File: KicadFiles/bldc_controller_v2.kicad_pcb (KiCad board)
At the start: 4 copper layers, 51.5 x 89 mm, 172 parts, among them J1 Conn_01x05_Male, J10 Conn_01x02_Female, J11 Conn_01x02_Female, J12 Conn_01x02_Female, J13 Conn_01x02_Female, J14 Conn_01x02_Female, J15 Conn_01x04_Male, J2 Conn_01x03_Male, J3 Conn_01x03_Male, J4 1935174, J5 Conn_01x02_Female, J9 Conn_01x02_Female, Q10 IRLB8721PBF, Q11 IRLB8721PBF, Q2 DMN65D8L-7, Q3 DMN65D8L-7, Q5 IRF4905, Q6 IRLB8721PBF, Q7 IRLB8721PBF, Q8 IRLB8721PBF, Q9 IRLB8721PBF, SW2 D6C40 F1 LFS, SW3 1301.9314, SW4 1301.9314, SW5 SW_Push_DPDT, U1 ATmega328P-PU, U2 uA7810, U3 LM7805_TO220, U4 MCP601-xP, U5 LM339, U6 IRS2004, U7 IRS2004, U8 IRS2004, U9 HCPL-181-00DE, Y1 9B-16.000MBBK-B

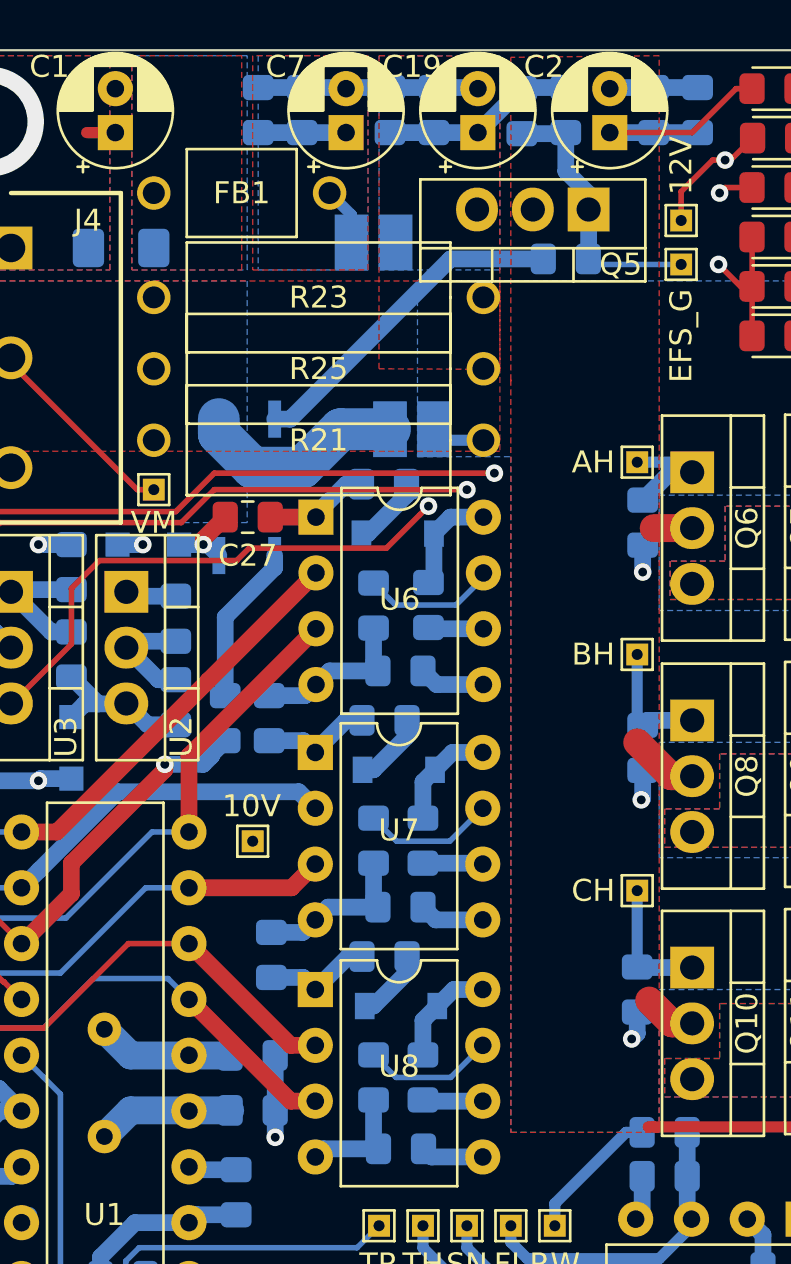
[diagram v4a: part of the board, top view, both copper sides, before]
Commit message: Almost Passes DRC
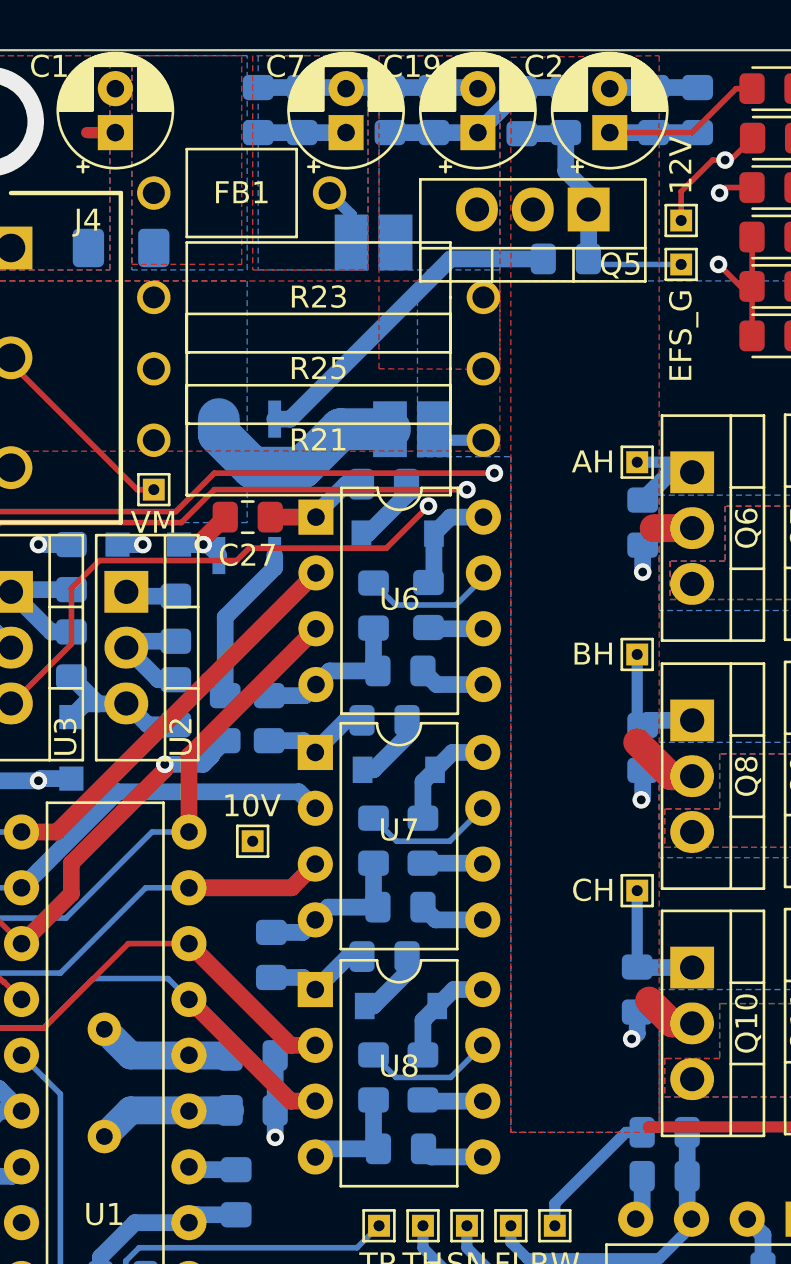
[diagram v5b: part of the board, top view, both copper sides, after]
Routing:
- net +5V: track 105.6 -> 106.7 mm
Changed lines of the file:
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@@
     (thickness 1.6)
     (drawings 76)
-    (tracks 751)
+    (tracks 753)
     (zones 0)
     (modules 172)
@@
     (35 F.Paste user)
     (36 B.SilkS user)
-    (37 F.SilkS user hide)
+    (37 F.SilkS user)
     (38 B.Mask user hide)
     (39 F.Mask user hide)
@@
   )
   (setup
-    (last_trace_width 1.27)
+    (last_trace_width 0.254)
     (user_trace_width 0.254)
     (user_trace_width 0.508)
@@
       (effects (font (size 1 1) (thickness 0.15)))
     )
+    (fp_line (start 1 1) (end -1 1) (layer F.CrtYd) (width 0.05))
+    (fp_line (start 1 1) (end 1 -1) (layer F.CrtYd) (width 0.05))
+    (fp_line (start -1 -1) (end -1 1) (layer F.CrtYd) (width 0.05))
+    (fp_line (start -1 -1) (end 1 -1) (layer F.CrtYd) (width 0.05))
+    (fp_line (start -0.7 0.7) (end -0.7 -0.7) (layer F.SilkS) (width 0.12))
+    (fp_line (start 0.7 0.7) (end -0.7 0.7) (layer F.SilkS) (width 0.12))
+    (fp_line (start 0.7 -0.7) (end 0.7 0.7) (layer F.SilkS) (width 0.12))
+    (fp_line (start -0.7 -0.7) (end 0.7 -0.7) (layer F.SilkS) (width 0.12))
     (fp_text user %R (at 0 -1.45) (layer F.Fab)
       (effects (font (size 1 1) (thickness 0.15)))
     )
-    (fp_line (start -0.7 -0.7) (end 0.7 -0.7) (layer F.SilkS) (width 0.12))
-    (fp_line (start 0.7 -0.7) (end 0.7 0.7) (layer F.SilkS) (width 0.12))
-    (fp_line (start 0.7 0.7) (end -0.7 0.7) (layer F.SilkS) (width 0.12))
-    (fp_line (start -0.7 0.7) (end -0.7 -0.7) (layer F.SilkS) (width 0.12))
-    (fp_line (start -1 -1) (end 1 -1) (layer F.CrtYd) (width 0.05))
-    (fp_line (start -1 -1) (end -1 1) (layer F.CrtYd) (width 0.05))
-    (fp_line (start 1 1) (end 1 -1) (layer F.CrtYd) (width 0.05))
-    (fp_line (start 1 1) (end -1 1) (layer F.CrtYd) (width 0.05))
     (pad 1 thru_hole rect (at 0 0) (size 1 1) (drill 0.5) (layers *.Cu *.Mask)
       (net 7 +12V))
@@
   (segment (start 117.25 90.73) (end 117.2975 90.73) (width 0.254) (layer F.Cu) (net 6))
   (segment (start 117.2975 90.73) (end 120 88.0275) (width 0.254) (layer F.Cu) (net 6))
-  (segment (start 136.25 72.5) (end 138.001148 70.748852) (width 0.254) (layer In1.Cu) (net 6))
-  (segment (start 136.25 81.75) (end 136.25 72.5) (width 0.254) (layer In1.Cu) (net 6))
-  (segment (start 138.001148 70.748852) (end 148.886164 70.748852) (width 0.254) (layer In1.Cu) (net 6))
-  (segment (start 148.886164 70.748852) (end 149.451849 70.748852) (width 0.254) (layer In1.Cu) (net 6))
   (via (at 149.451849 70.748852) (size 0.8) (drill 0.4) (layers F.Cu B.Cu) (net 6))
   (segment (start 150.452997 71.75) (end 149.451849 70.748852) (width 0.254) (layer F.Cu) (net 6))
@@
   (segment (start 116.7 108.25) (end 117.73 109.28) (width 0.762) (layer B.Cu) (net 6))
   (segment (start 114.75 108.25) (end 116.7 108.25) (width 0.762) (layer B.Cu) (net 6))
+  (segment (start 144.498852 70.748852) (end 144.5 70.75) (width 0.254) (layer In1.Cu) (net 6))
+  (segment (start 138.001148 70.748852) (end 144.498852 70.748852) (width 0.254) (layer In1.Cu) (net 6))
+  (segment (start 136.25 81.75) (end 136.25 72.5) (width 0.254) (layer In1.Cu) (net 6))
+  (segment (start 136.25 72.5) (end 138.001148 70.748852) (width 0.254) (layer In1.Cu) (net 6))
+  (segment (start 144.498852 70.748852) (end 145.75 72) (width 0.254) (layer In1.Cu) (net 6))
+  (segment (start 145.75 72) (end 148.25 72) (width 0.254) (layer In1.Cu) (net 6))
+  (segment (start 148.25 71.950701) (end 149.451849 70.748852) (width 0.254) (layer In1.Cu) (net 6))
+  (segment (start 148.25 72) (end 148.25 71.950701) (width 0.254) (layer In1.Cu) (net 6))
   (segment (start 122.7 85.85) (end 122.5 85.65) (width 0.762) (layer B.Cu) (net 7))
   (segment (start 124.75 85.85) (end 122.7 85.85) (width 0.762) (layer B.Cu) (net 7))
@@
   (segment (start 150.975 67.25) (end 149.750006 67.25) (width 0.254) (layer F.Cu) (net 8))
   (segment (start 131.13 76.87) (end 131.13 82.25) (width 0.254) (layer In1.Cu) (net 8))
-  (segment (start 147 67.5) (end 146 68.5) (width 0.254) (layer In1.Cu) (net 8))
-  (segment (start 149.500006 67.5) (end 147 67.5) (width 0.254) (layer In1.Cu) (net 8))
-  (segment (start 146 68.5) (end 146 69.125) (width 0.254) (layer In1.Cu) (net 8))
-  (segment (start 146 69.125) (end 145.125 70) (width 0.254) (layer In1.Cu) (net 8))
-  (segment (start 145.125 70) (end 138 70) (width 0.254) (layer In1.Cu) (net 8))
   (segment (start 138 70) (end 131.13 76.87) (width 0.254) (layer In1.Cu) (net 8))
+  (segment (start 144.5 70) (end 138 70) (width 0.254) (layer In1.Cu) (net 8))
+  (segment (start 149.500006 67.5) (end 147 67.5) (width 0.254) (layer In1.Cu) (net 8))
+  (segment (start 147 67.5) (end 144.5 70) (width 0.254) (layer In1.Cu) (net 8))
   (via (at 119.5 122.5) (size 0.8) (drill 0.4) (layers F.Cu B.Cu) (net 9))
   (segment (start 146.3 140.975) (end 143.9 140.975) (width 0.254) (layer B.Cu) (net 9))
@@
   (segment (start 120 87.475) (end 119.075 87.475) (width 0.762) (layer B.Cu) (net 86))
   (zone (net 2) (net_name +BATT) (layer F.Cu) (hatch edge 0.508)
+    (priority 1)
     (connect_pads (clearance 0.508))
     (min_thickness 0.254)
@@
   )
   (zone (net 2) (net_name +BATT) (layer B.Cu) (hatch edge 0.508)
+    (priority 1)
     (connect_pads (clearance 0.508))
     (min_thickness 0.254)
@@
   )
   (zone (net 32) (net_name "Net-(F1-Pad1)") (layer B.Cu) (hatch edge 0.508)
+    (priority 2)
     (connect_pads (clearance 0.508))
     (min_thickness 0.254)
@@
   )
   (zone (net 32) (net_name "Net-(F1-Pad1)") (layer F.Cu) (hatch edge 0.508)
+    (priority 2)
     (connect_pads (clearance 0.508))
     (min_thickness 0.254)
@@
     (polygon
       (pts
-        (xy 122.75 71) (xy 127.75 71) (xy 127.75 61.25) (xy 122.75 61.25)
+        (xy 122.75 70.75) (xy 127.75 70.75) (xy 127.75 61.25) (xy 122.75 61.25)
       )
     )
   )
   (zone (net 7) (net_name +12V) (layer F.Cu) (hatch edge 0.508)
+    (priority 3)
     (connect_pads (clearance 0.508))
     (min_thickness 0.254)
@@
   )
   (zone (net 7) (net_name +12V) (layer B.Cu) (hatch edge 0.508)
+    (priority 3)
     (connect_pads (clearance 0.508))
     (min_thickness 0.254)
@@
   )
   (zone (net 12) (net_name /V_MOTOR) (layer F.Cu) (hatch edge 0.508)
+    (priority 4)
     (connect_pads (clearance 0.508))
     (min_thickness 0.254)
@@
   )
   (zone (net 45) (net_name /I_RAW) (layer B.Cu) (hatch edge 0.508)
+    (priority 6)
     (connect_pads (clearance 0.508))
     (min_thickness 0.254)
@@
   )
   (zone (net 1) (net_name GNDPWR) (layer Gnd.Cu) (hatch edge 0.508)
+    (priority 10)
     (connect_pads (clearance 0.508))
     (min_thickness 0.254)
@@
     (polygon
       (pts
-        (xy 113.25 82.5) (xy 164.25 82.5) (xy 164.25 63.5) (xy 162 61.25) (xy 115.5 61.25)
+        (xy 113.25 82.5) (xy 164.25 82.5) (xy 164.25 61.25) (xy 162 61.25) (xy 115.5 61.25)
         (xy 113.25 63.5)
       )
@@
   )
   (zone (net 4) (net_name GNDD) (layer Gnd.Cu) (hatch edge 0.508)
+    (priority 11)
     (connect_pads (clearance 0.508))
     (min_thickness 0.254)
@@
   )
   (zone (net 3) (net_name VBUS) (layer F.Cu) (hatch edge 0.508)
+    (priority 5)
     (connect_pads (clearance 0.508))
     (min_thickness 0.254)
@@
     (polygon
       (pts
-        (xy 140 76) (xy 140 110.25) (xy 146.75 110.25) (xy 146.75 78.75) (xy 146.75 61.25)
-        (xy 140 61.325) (xy 140 76.075)
+        (xy 146.75 110.25) (xy 140 110.25) (xy 140 61.325) (xy 146.75 61.25)
       )
     )
@@
   )
   (zone (net 8) (net_name +10V) (layer In1.Cu) (hatch edge 0.508)
+    (priority 3)
     (connect_pads (clearance 0.508))
     (min_thickness 0.254)
@@
   )
   (zone (net 6) (net_name +5V) (layer In1.Cu) (hatch edge 0.508)
+    (priority 2)
     (connect_pads (clearance 0.508))
     (min_thickness 0.254)
@@
     (polygon
       (pts
-        (xy 117.25 89.5) (xy 113.25 89.5) (xy 113.25 149.75) (xy 152 149.75) (xy 152 113.5)
-        (xy 120 113.5) (xy 120 89.5) (xy 117 89.5)
+        (xy 120 113.5) (xy 152 113.5) (xy 152 149.75) (xy 113.25 149.75) (xy 113.25 89.5)
+        (xy 120 89.5)
       )
     )
   )
   (zone (net 7) (net_name +12V) (layer In1.Cu) (hatch edge 0.508)
+    (priority 1)
     (connect_pads (clearance 0.508))
     (min_thickness 0.254)
@@
     (polygon
       (pts
-        (xy 136 61.5) (xy 136 61.25) (xy 113.25 61.25) (xy 113.25 89) (xy 126.25 89)
-        (xy 126.25 80.25) (xy 136 80.25) (xy 136 61.25)
+        (xy 136 80.25) (xy 126.25 80.25) (xy 126.25 89) (xy 113.25 89) (xy 113.25 61.25)
+        (xy 136 61.25)
       )
     )
@@
   )
   (zone (net 1) (net_name GNDPWR) (layer B.Cu) (hatch edge 0.508)
+    (priority 5)
     (connect_pads (clearance 0.508))
     (min_thickness 0.254)
@@
   )
   (zone (net 12) (net_name /V_MOTOR) (layer F.Cu) (hatch edge 0.508)
+    (priority 2)
     (connect_pads (clearance 0.508))
     (min_thickness 0.254)
@@
   )
   (zone (net 6) (net_name +5V) (layer In1.Cu) (hatch edge 0.508)
+    (priority 2)
     (connect_pads (clearance 0.508))
     (min_thickness 0.254)
@@
   )
   (zone (net 12) (net_name /V_MOTOR) (layer B.Cu) (hatch edge 0.508)
+    (priority 4)
     (connect_pads (clearance 0.508))
     (min_thickness 0.254)
